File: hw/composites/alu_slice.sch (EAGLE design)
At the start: 10 parts, among them CON2 GENERIC-2X10

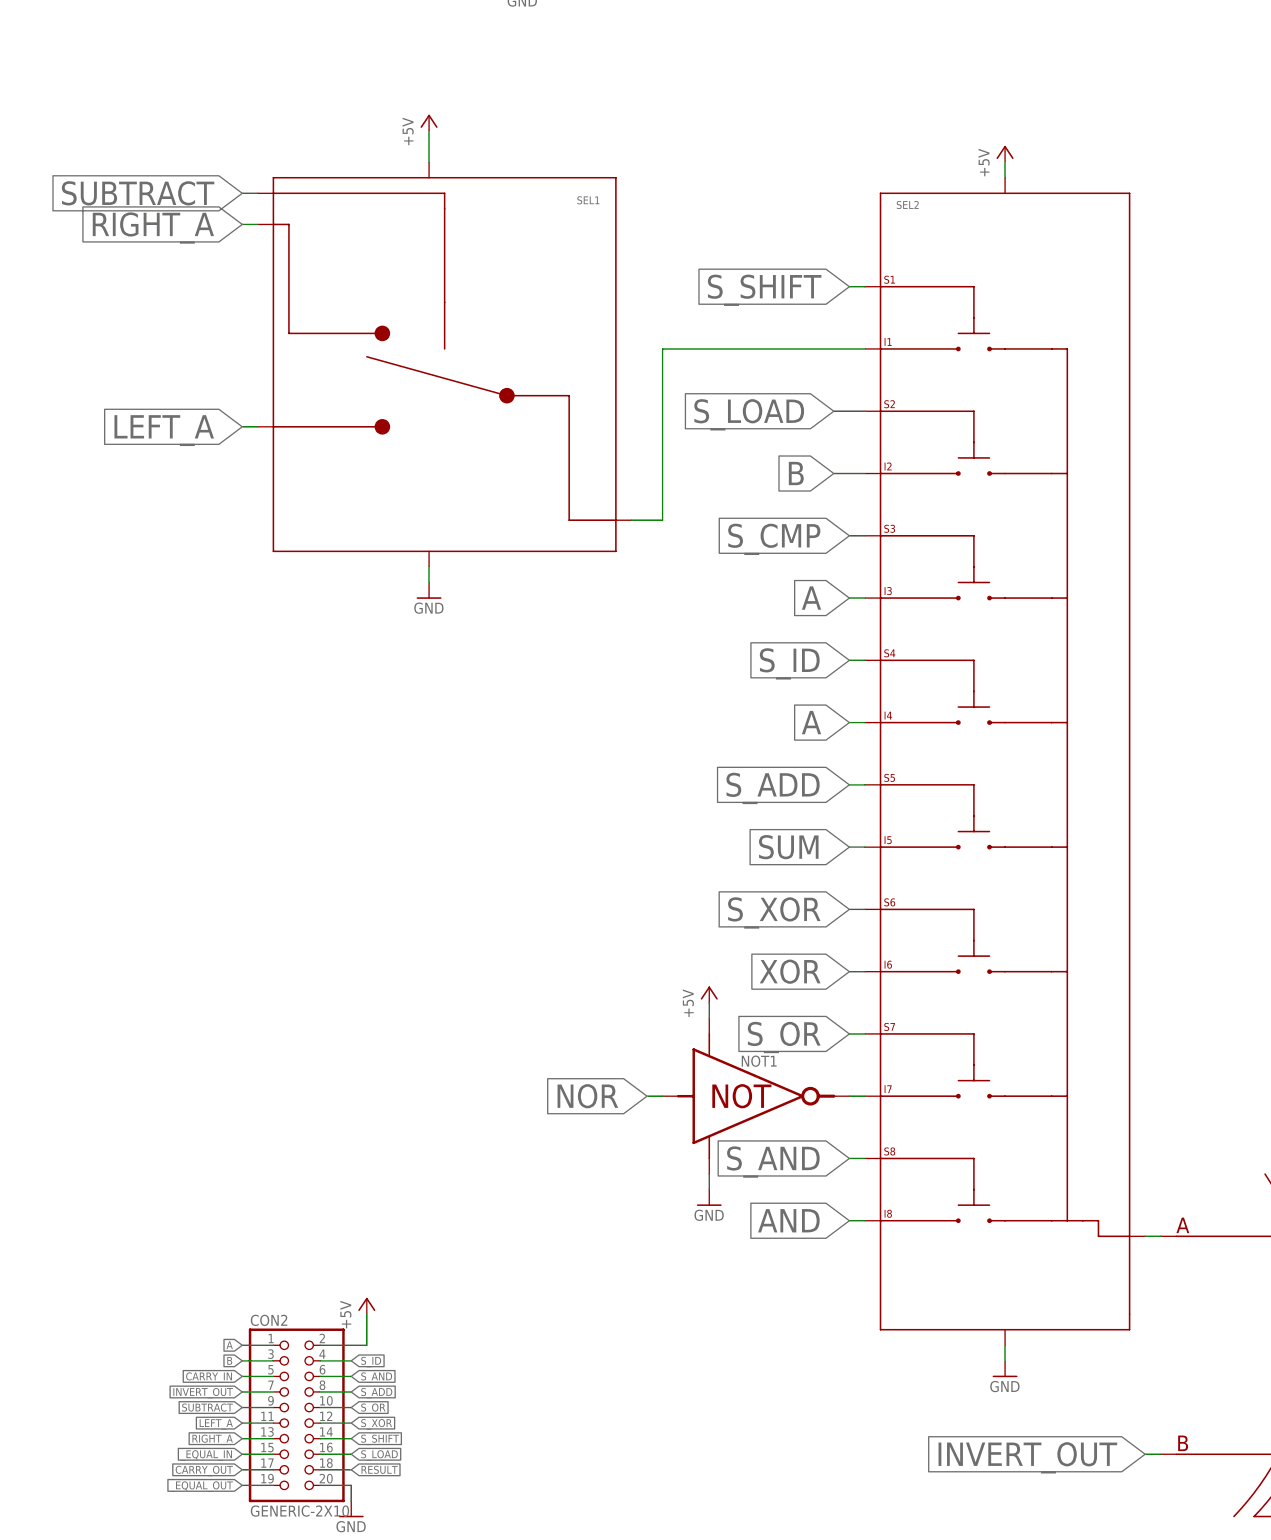
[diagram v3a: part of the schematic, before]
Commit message: changes CMP and ID to use same selector
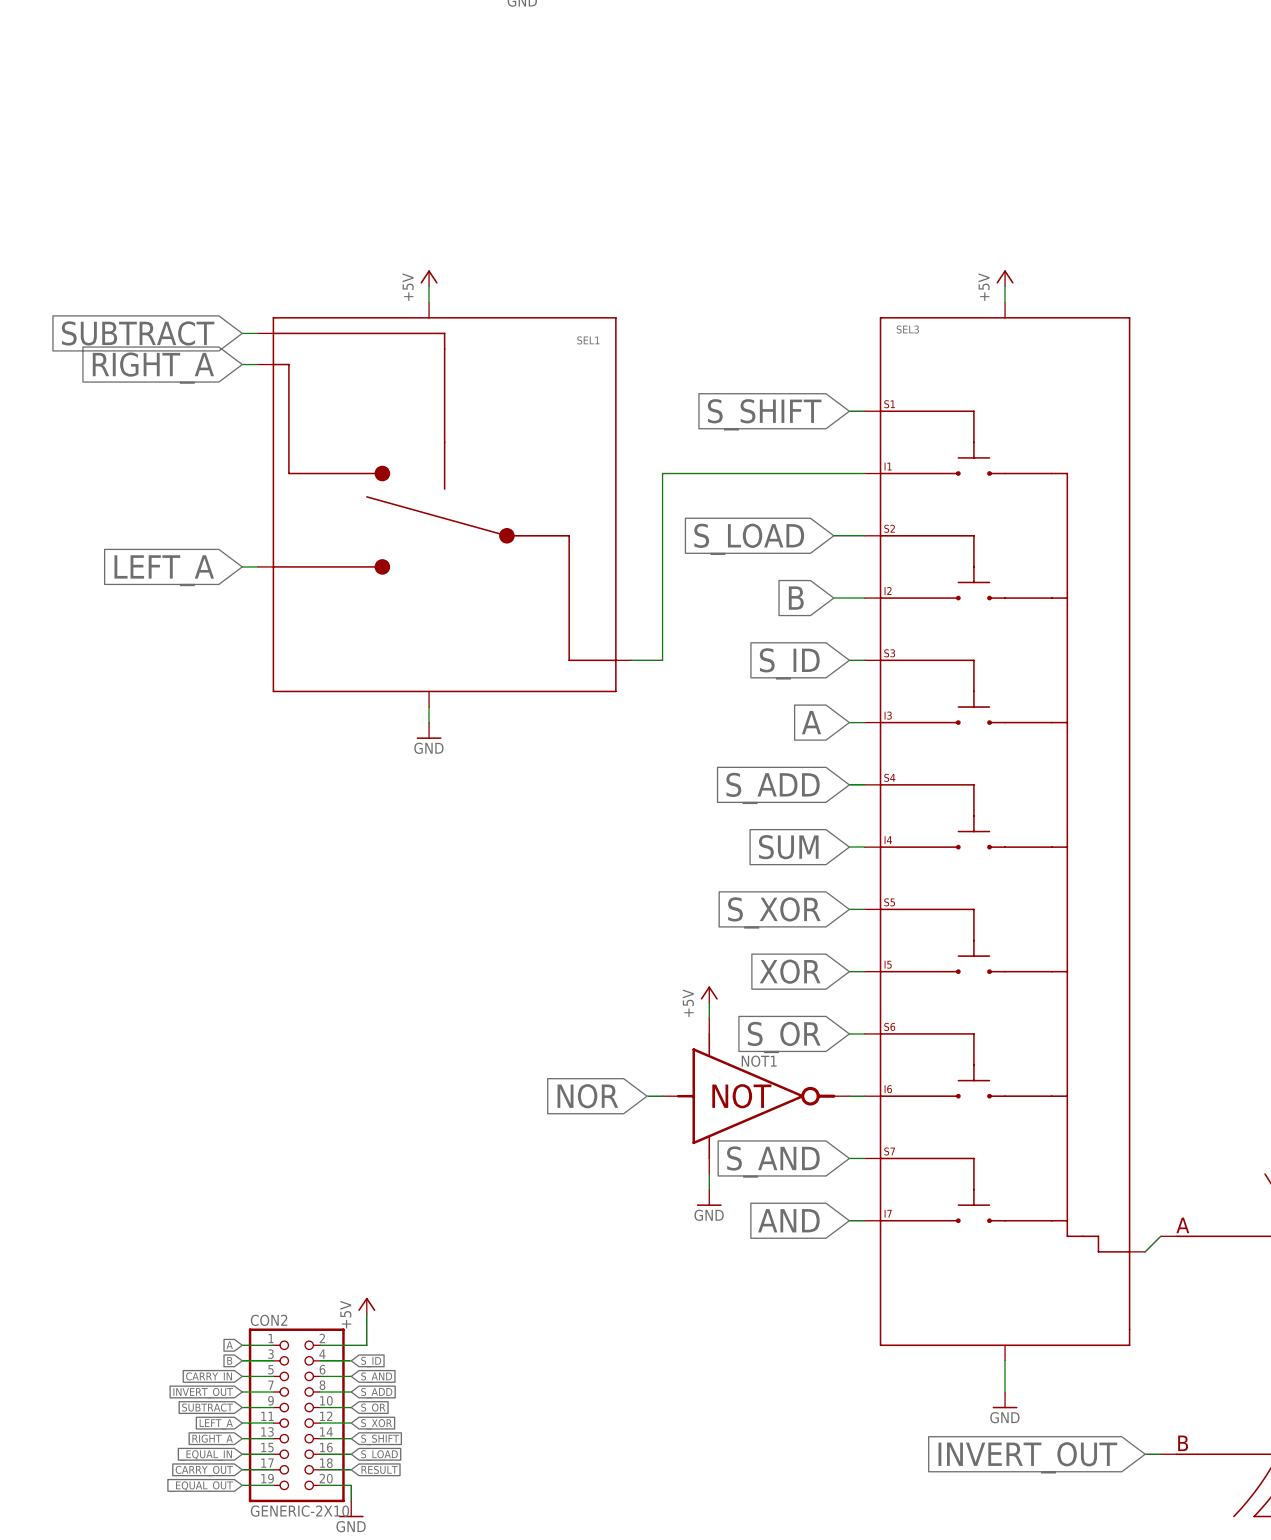
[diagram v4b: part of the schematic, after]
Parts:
- removed SEL2: 8_BIT_SELECT, p.peter-gator:8_BIT_SELECT
- added SEL3: 7_VAL_SELECT, p.peter-gator:7_VAL_SELECT
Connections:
- removed net S_CMP: SEL2.S3
- net +5V: now also SEL3._VP; no longer SEL2._VP
- net A: now also SEL3.I3; no longer SEL2.I3, SEL2.I4
- net AND: now also SEL3.I7; no longer SEL2.I8
- net B: now also SEL3.I2; no longer SEL2.I2
- net GND: now also SEL3._VN; no longer SEL2._VN
- net N$1: now also SEL3.OUT; no longer SEL2.OUT
- net N$3: now also SEL3.I6; no longer SEL2.I7
- net N$5: now also SEL3.I1; no longer SEL2.I1
- net SUM: now also SEL3.I4; no longer SEL2.I5
- net S_ADD: now also SEL3.S4; no longer SEL2.S5
- net S_AND: now also SEL3.S7; no longer SEL2.S8
- net S_ID: now also SEL3.S3; no longer SEL2.S4
- net S_LOAD: now also SEL3.S2; no longer SEL2.S2
- net S_OR: now also SEL3.S6; no longer SEL2.S7
- net S_SHIFT: now also SEL3.S1; no longer SEL2.S1
- net S_XOR: now also SEL3.S5; no longer SEL2.S6
- net XOR: now also SEL3.I5; no longer SEL2.I6
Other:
- moved on the sheet: SEL1

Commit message: Add led output and prepare first alu slice
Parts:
- added L1: (no value), p.peter-leds:LED0805
- added PCB1: PCB_DP_SQUARE-5X5, dp_pcb:PCB_DP_SQUARE-5X5
- added R1: 1k, p.peter-rcl:R-EU-MARKEDR0603
- added U$1, U$2, U$3, U$4, U$5: LEDDRIVER, p.peter-gator:LEDDRIVER
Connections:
- new net N$6: L1.C, R1.2
- net +5V: now also L1.A, U$1._VP, U$2._VP, U$3._VP, U$4._VP, U$5._VP
- net A: now also U$1.A
- net B: now also U$2.A
- net CARRY_IN: now also U$3.A
- net CARRY_OUT: now also U$5.A
- net GND: now also R1.1, U$1._VN, U$2._VN, U$3._VN, U$4._VN, U$5._VN
- net RESULT: now also U$4.A
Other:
- moved on the sheet: CON2, NOT1, XOR1
